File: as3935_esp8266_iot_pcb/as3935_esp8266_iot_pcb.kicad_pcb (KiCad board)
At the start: 2 copper layers, 50 x 100 mm, 41 parts, among them K1 RELAY_2RT, K2 RELAY_2RT, P1 CONN_01X02, P2 CONN_01X02, P3 CONN_01X02, P4 CONN_01X08, P5 CONN_01X07, P6 CONN_01X03, P7 CONN_01X03, P8 CONN_01X06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

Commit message: just simbols
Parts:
- removed REF** (x2): Symbol_HighVoltage_Type2_CopperTop_VerySmall, Symbols:Symbol_HighVoltage_Type2_CopperTop_VerySmall
- removed REF**: Symbol_CC-Noncommercial_CopperTop_Small, Symbols:Symbol_CC-Noncommercial_CopperTop_Small
- added REF05: Symbol_ESD-Logo_CopperTop, Symbols:Symbol_ESD-Logo_CopperTop, F.Cu at (40.5, 80.0)
- added REF054: Symbol_OSHW-Logo_SilkScreen, Symbols:Symbol_OSHW-Logo_SilkScreen, F.Cu at (45.8, 67.8)
- added REF220: Symbol_Highvoltage_Type1_CopperTop_Small, Symbols:Symbol_Highvoltage_Type1_CopperTop_Small, F.Cu at (23.2, 120.0)

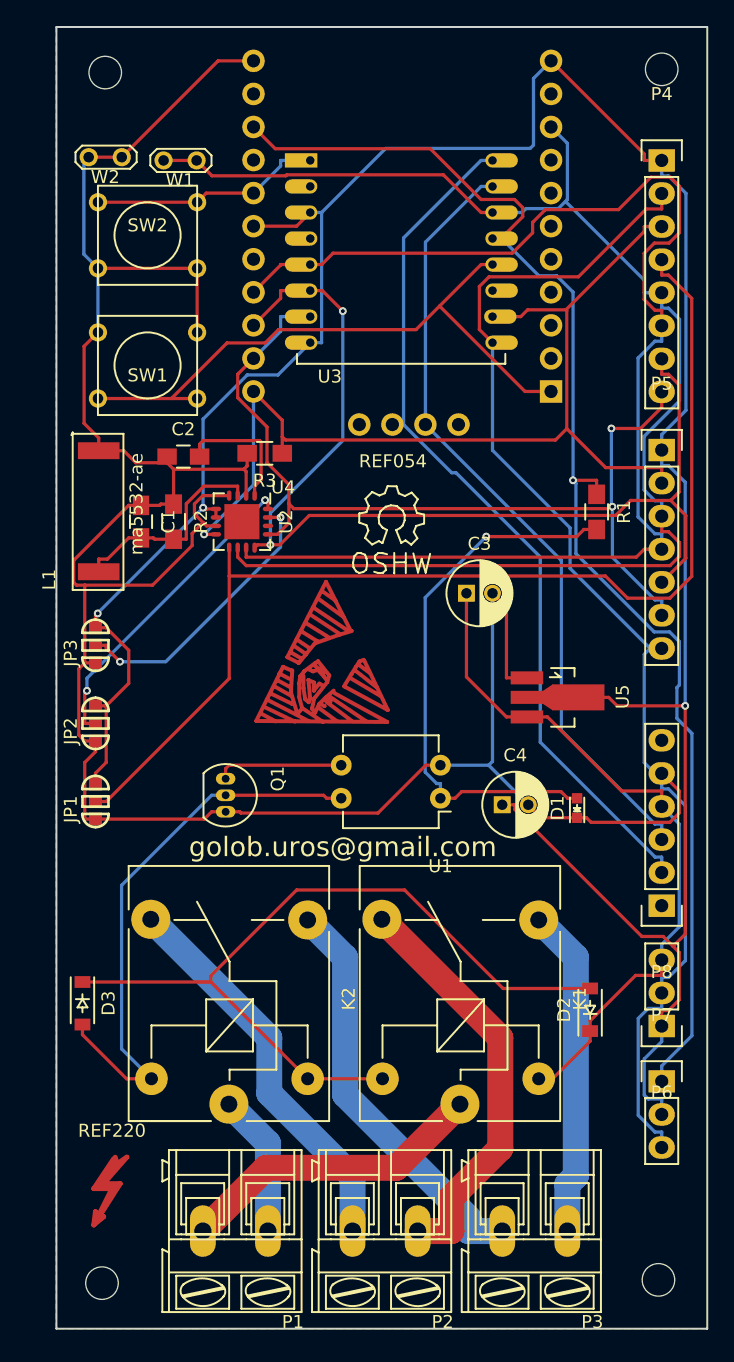
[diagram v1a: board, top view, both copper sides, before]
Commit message: copper fill
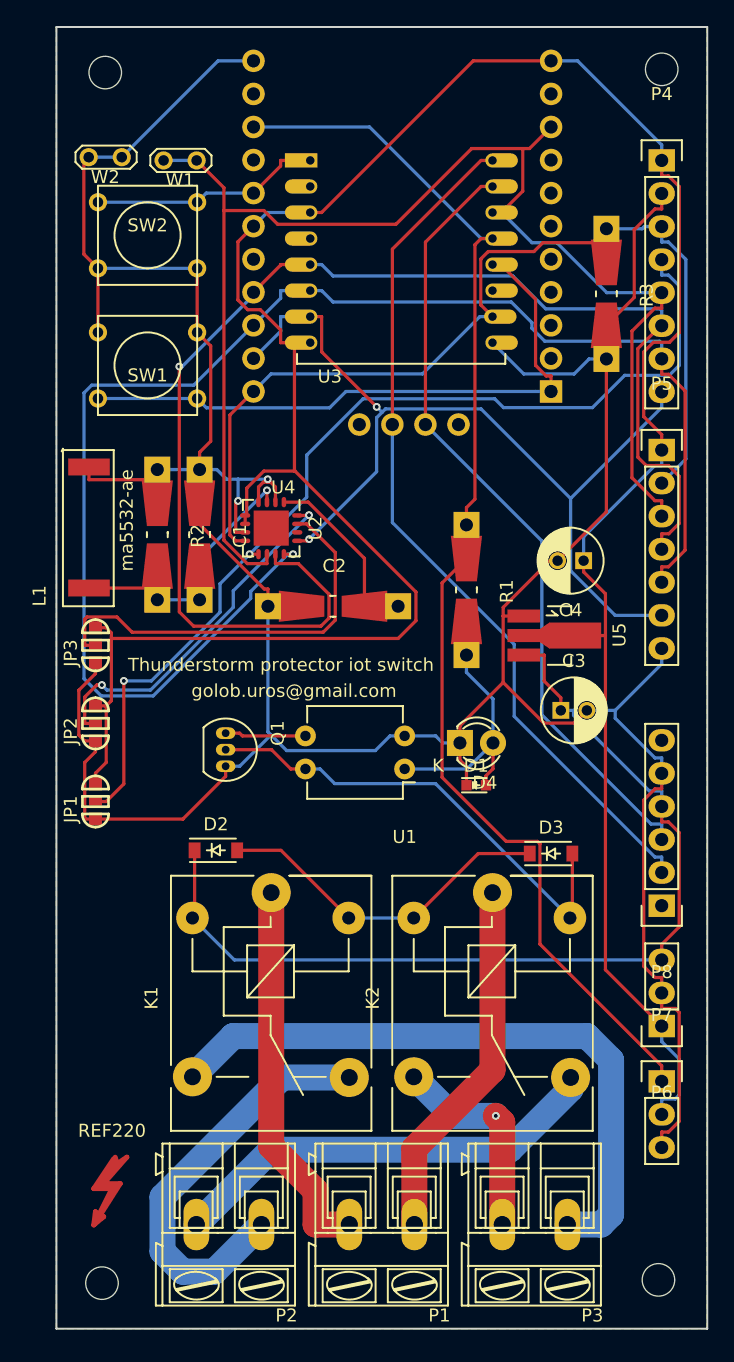
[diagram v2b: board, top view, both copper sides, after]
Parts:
- removed REF05: Symbol_ESD-Logo_CopperTop, Symbols:Symbol_ESD-Logo_CopperTop
- removed REF054: Symbol_OSHW-Logo_SilkScreen, Symbols:Symbol_OSHW-Logo_SilkScreen
- added D4: LED, LEDs:LED-3MM, F.Cu at (51.0, 85.0)
- C1, C2: footprint Capacitors_SMD_local:C_0805_HandSoldering -> Resistors_Universal:Resistor_SMD+THTuniversal_0805to1206_RM10_HandSoldering
- JP1: value JUMPER3 -> i2c/spi
- JP2: value JUMPER3 -> add1
- JP3: value JUMPER3 -> add0
- R1, R2, R3: footprint Resistors_SMD:R_0805_HandSoldering -> Resistors_Universal:Resistor_SMD+THTuniversal_0805to1206_RM10_HandSoldering
- moved D3 37.8 mm to (58.0, 93.5), turned to 0 degrees
- moved D2 31.3 mm to (32.2, 93.2), turned to 0 degrees
- moved R3 29.0 mm to (62.2, 50.5), turned to 270 degrees
- moved K2 26.0 mm to (53.5, 96.5), turned to 270 degrees
- moved K1 21.8 mm to (36.5, 96.5), turned to 270 degrees
- moved C4 19.8 mm to (60.5, 71.0), turned to 180 degrees
- moved C2 16.3 mm to (41.2, 74.5)
- moved P2 12.0 mm to (35.8, 122.0)
- moved R1 11.7 mm to (51.5, 73.2)
- moved C3 11.6 mm to (58.8, 82.5)
- moved P1 11.3 mm to (47.5, 122.0)
- moved D1 7.95 mm to (52.2, 88.2), turned to 0 degrees
- moved U5 4.76 mm to (58.2, 76.8)
- moved C1 4.61 mm to (31.0, 69.0)
- moved U1 3.55 mm to (46.8, 87.0)
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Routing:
- net Net-(D2-Pad2): track 61.6 -> 26.7 mm
- net /miso: track 82.2 -> 114.5 mm, vias 2 -> 1
- net Net-(K1-Pad3): track 25.4 -> 49.8 mm
- net Net-(D1-Pad2): track 42.3 -> 21.3 mm, vias 1 -> 0
- net +5V: track 54.0 -> 73.9 mm
- net GND: track 291.6 -> 273.0 mm, vias 0 -> 2
- net Net-(K2-Pad5): track 11.0 -> 28.0 mm
- net Net-(K2-Pad3): track 31.6 -> 16.1 mm, vias 0 -> 1
- net /add0: track 21.7 -> 32.0 mm, vias 2 -> 0
- net /si: track 86.8 -> 76.8 mm, vias 0 -> 2
- net Net-(C1-Pad2): track 16.4 -> 25.1 mm, vias 0 -> 1
- net /to_sw: track 104.0 -> 97.2 mm, vias 1 -> 0
- net Net-(D3-Pad2): track 43.1 -> 36.8 mm
- net Net-(K1-Pad5): track 23.8 -> 29.5 mm
- net Net-(C2-Pad2): track 10.2 -> 14.2 mm
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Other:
- board text added: "Thunderstorm protector iot switch"

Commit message: copper fill, smd transistor, resistors and capacitors on universal pads for smd 805 or trough hole
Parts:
- added Q2: BC849, SOT-23, F.Cu at (29.0, 85.2)
- JP1: value i2c/spi -> JUMPER3
- JP2: value add1 -> JUMPER3
- JP3: value add0 -> JUMPER3
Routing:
- net Net-(D3-Pad2): track 36.8 -> 41.1 mm
- net Net-(Q1-Pad1): track 6.22 -> 9.27 mm
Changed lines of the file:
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@@
 (kicad_pcb (version 4) (host pcbnew "(2015-08-08 BZR 6073)-product")
   (general
-    (links 121)
+    (links 124)
     (no_connects 0)
-    (area 6.368712 28.22488 75.583584 131.47418)
+    (area 19.924999 29.924999 70.075001 130.075001)
     (thickness 1.6)
     (drawings 6)
-    (tracks 501)
+    (tracks 506)
     (zones 0)
-    (modules 40)
+    (modules 41)
     (nets 48)
   )
@@
       (effects (font (size 1 1) (thickness 0.15)))
     )
-    (fp_text value i2c/spi (at 0.1 -2.1 270) (layer F.Fab)
+    (fp_text value JUMPER3 (at 0.1 -2.1 270) (layer F.Fab)
       (effects (font (size 1 1) (thickness 0.15)))
     )
@@
       (effects (font (size 1 1) (thickness 0.15)))
     )
-    (fp_text value add1 (at 0.1 -2.1 270) (layer F.Fab)
+    (fp_text value JUMPER3 (at 0.1 -2.1 270) (layer F.Fab)
       (effects (font (size 1 1) (thickness 0.15)))
     )
@@
       (effects (font (size 1 1) (thickness 0.15)))
     )
-    (fp_text value add0 (at 0.1 -2.1 270) (layer F.Fab)
+    (fp_text value JUMPER3 (at 0.1 -2.1 270) (layer F.Fab)
       (effects (font (size 1 1) (thickness 0.15)))
     )
@@
     (pad 2 thru_hole rect (at 5.00126 0 90) (size 1.99898 1.99898) (drill 1.00076) (layers *.Cu *.Mask F.SilkS)
       (net 2 GND))
+  )
+  (module SOT-23 (layer F.Cu)
+    (at 29 85.25 180)
+    (descr "SOT-23, Standard")
+    (tags SOT-23)
+    (attr smd)
+    (fp_text reference Q2 (at 0 -2.25 180) (layer F.SilkS)
+      (effects (font (size 1 1) (thickness 0.15)))
+    )
+    (fp_text value BC849 (at 0 2.3 180) (layer F.Fab)
+      (effects (font (size 1 1) (thickness 0.15)))
+    )
+    (fp_line (start -1.65 -1.6) (end 1.65 -1.6) (layer F.CrtYd) (width 0.05))
+    (fp_line (start 1.65 -1.6) (end 1.65 1.6) (layer F.CrtYd) (width 0.05))
+    (fp_line (start 1.65 1.6) (end -1.65 1.6) (layer F.CrtYd) (width 0.05))
+    (fp_line (start -1.65 1.6) (end -1.65 -1.6) (layer F.CrtYd) (width 0.05))
+    (fp_line (start 1.29916 -0.65024) (end 1.2509 -0.65024) (layer F.SilkS) (width 0.15))
+    (fp_line (start -1.49982 0.0508) (end -1.49982 -0.65024) (layer F.SilkS) (width 0.15))
+    (fp_line (start -1.49982 -0.65024) (end -1.2509 -0.65024) (layer F.SilkS) (width 0.15))
+    (fp_line (start 1.29916 -0.65024) (end 1.49982 -0.65024) (layer F.SilkS) (width 0.15))
+    (fp_line (start 1.49982 -0.65024) (end 1.49982 0.0508) (layer F.SilkS) (width 0.15))
+    (pad 1 smd rect (at -0.95 1.00076 180) (size 0.8001 0.8001) (layers F.Cu F.Paste F.Mask)
+      (net 28 "Net-(Q1-Pad1)"))
+    (pad 2 smd rect (at 0.95 1.00076 180) (size 0.8001 0.8001) (layers F.Cu F.Paste F.Mask)
+      (net 2 GND))
+    (pad 3 smd rect (at 0 -0.99822 180) (size 0.8001 0.8001) (layers F.Cu F.Paste F.Mask)
+      (net 8 "Net-(D3-Pad2)"))
+    (model Housings_SOT-23_SOT-143_TSOT-6.3dshapes/SOT-23.wrl
+      (at (xyz 0 0 0))
+      (scale (xyz 1 1 1))
+      (rotate (xyz 0 0 0))
+    )
   )
   (gr_text "Thunderstorm protector iot switch" (at 37.25 79) (layer F.SilkS)
@@
   (segment (start 37.25 93.25) (end 33.885 93.25) (width 0.25) (layer F.Cu) (net 7))
   (segment (start 42.45 98.45) (end 37.25 93.25) (width 0.25) (layer F.Cu) (net 7))
+  (segment (start 29 86.24822) (end 29.75178 86.24822) (width 0.25) (layer F.Cu) (net 8) (status 400000))
+  (segment (start 30.48 85.52) (end 33 85.52) (width 0.25) (layer F.Cu) (net 8) (status 800000))
+  (segment (start 29.75178 86.24822) (end 30.48 85.52) (width 0.25) (layer F.Cu) (net 8))
   (segment (start 59.635 98.265) (end 59.635 93.5) (width 0.25) (layer F.Cu) (net 8))
   (segment (start 59.45 98.45) (end 59.635 98.265) (width 0.25) (layer F.Cu) (net 8))
@@
   (segment (start 65.6826 91.2311) (end 57.2913 82.8398) (width 0.25) (layer B.Cu) (net 26))
   (segment (start 66.5 91.2311) (end 65.6826 91.2311) (width 0.25) (layer B.Cu) (net 26))
+  (segment (start 29.95 84.24924) (end 32.99924 84.24924) (width 0.25) (layer F.Cu) (net 28) (status C00000))
+  (segment (start 32.99924 84.24924) (end 33 84.25) (width 0.25) (layer F.Cu) (net 28) (status C00000))
   (segment (start 34.2859 84.46) (end 34.0759 84.25) (width 0.25) (layer F.Cu) (net 28))
   (segment (start 39.13 84.46) (end 34.2859 84.46) (width 0.25) (layer F.Cu) (net 28))
